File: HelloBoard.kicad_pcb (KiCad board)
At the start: 2 copper layers, 106.3 x 77 mm, 52 parts, among them J1 USB_B_Micro, J2 Conn_01x04_Pin, J3 Conn_01x04_Pin, J4 Conn_02x08_Top_Bottom, J5 Conn_01x02, SW1 SW_Push, SW2 SW_Push, U1 STM32F103C8T6, U2 AMS1117-3.3, U3 TMP235A2DCKR, U4 ADXL343, Y1 16MHz

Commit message: about to run DRC
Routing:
- net /PC_14: track 6.47 -> 71.3 mm, vias 0 -> 10
- net /PC_15: track 6.70 -> 66.6 mm, vias 0 -> 12
- net /PA_9: track 0.00 -> 53.5 mm, vias 0 -> 7
- net /PB_5: track 0.00 -> 50.4 mm, vias 0 -> 4
- net /PA_10: track 0.00 -> 47.8 mm, vias 0 -> 6
- net /PB_4: track 0.00 -> 45.1 mm, vias 0 -> 4
- net /PB_3: track 0.00 -> 40.2 mm, vias 0 -> 6
- net +3.3V: track 266.7 -> 270.2 mm

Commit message: the router ?
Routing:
- net unconnected-(J1-Shield-Pad6)_2: track 0.00 -> 18.0 mm, vias 0 -> 3
- net /PA_10: track 47.8 -> 49.3 mm
- net /PA_9: track 53.5 -> 55.0 mm, vias 7 -> 6
- net /7SEG_A: vias 3 -> 2

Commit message: minor silkscreen edits
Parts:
- renumbered SW1 to NRST
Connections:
- net Net-(J5-Pin_1) renamed /ADXL_INT1
- net Net-(J5-Pin_2) renamed /ADXL_INT2
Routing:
- net unconnected-(J1-Shield-Pad6)_2: track 18.0 -> 0.16 mm, vias 3 -> 0
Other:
- board text added: "16x2 LCD"
- board text added: "3.3V"
- board text added: "5V"
- board text added: "7 SEGMENT DISPLAY"
- board text added: "ADXL343"
- board text added: "GND"
- board text added: "INT1"
- board text added: "INT2"
- board text added: "LCD CONTRAST"
- board text added: "PA10"
- board text added: "PA11"
- board text added: "PA12"
- board text added: "PA7"
- board text added: "PA8"
- board text added: "PA9"
- board text added: "PB1"
- board text added: "PB2"
- board text added: "PB3"
- board text added: "PB4"
- board text added: "PB5"
- board text added: "PC14"
- board text added: "PC15"
- board text added: "SCL"
- board text added: "SDA"
- board text added: "SWCLK"
- board text added: "SWDIO"
- board text added: "TMP235"
- board text added: "USER BUTTON"

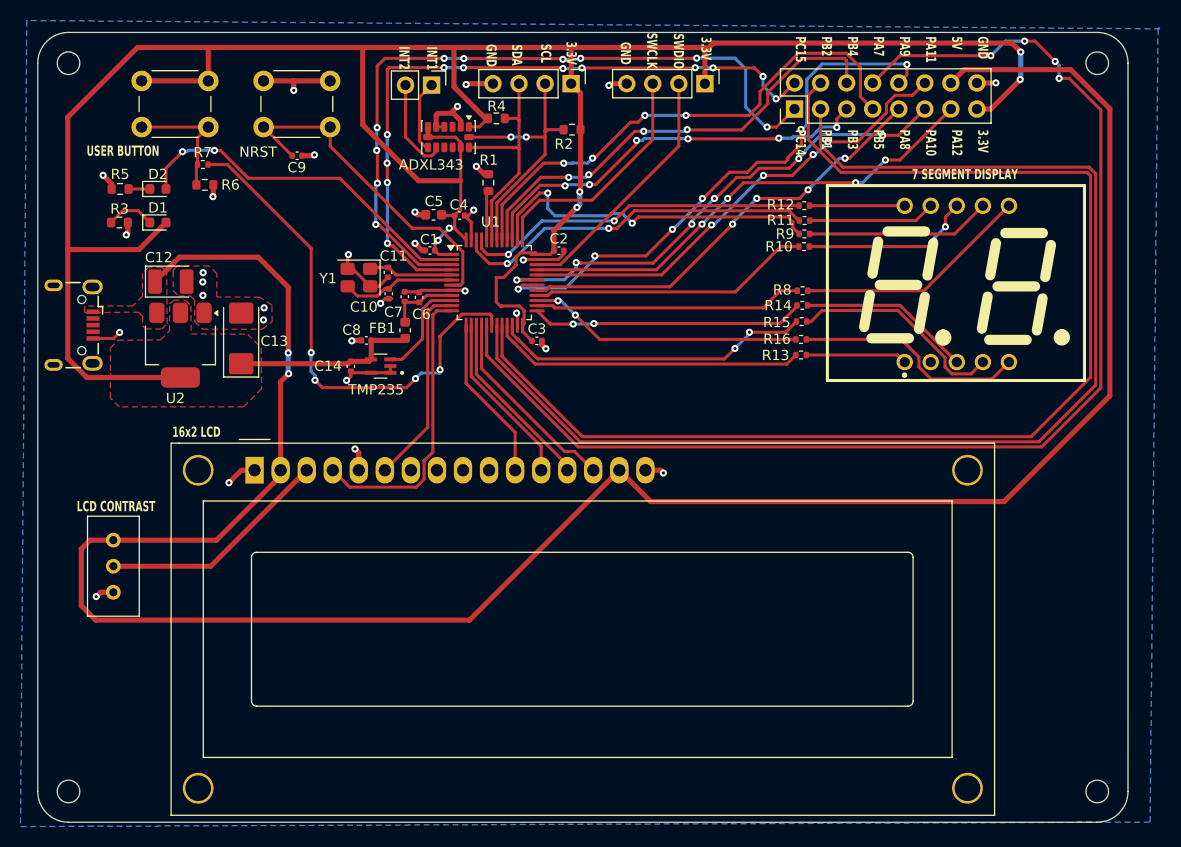
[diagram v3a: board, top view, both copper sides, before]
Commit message: minor via edits
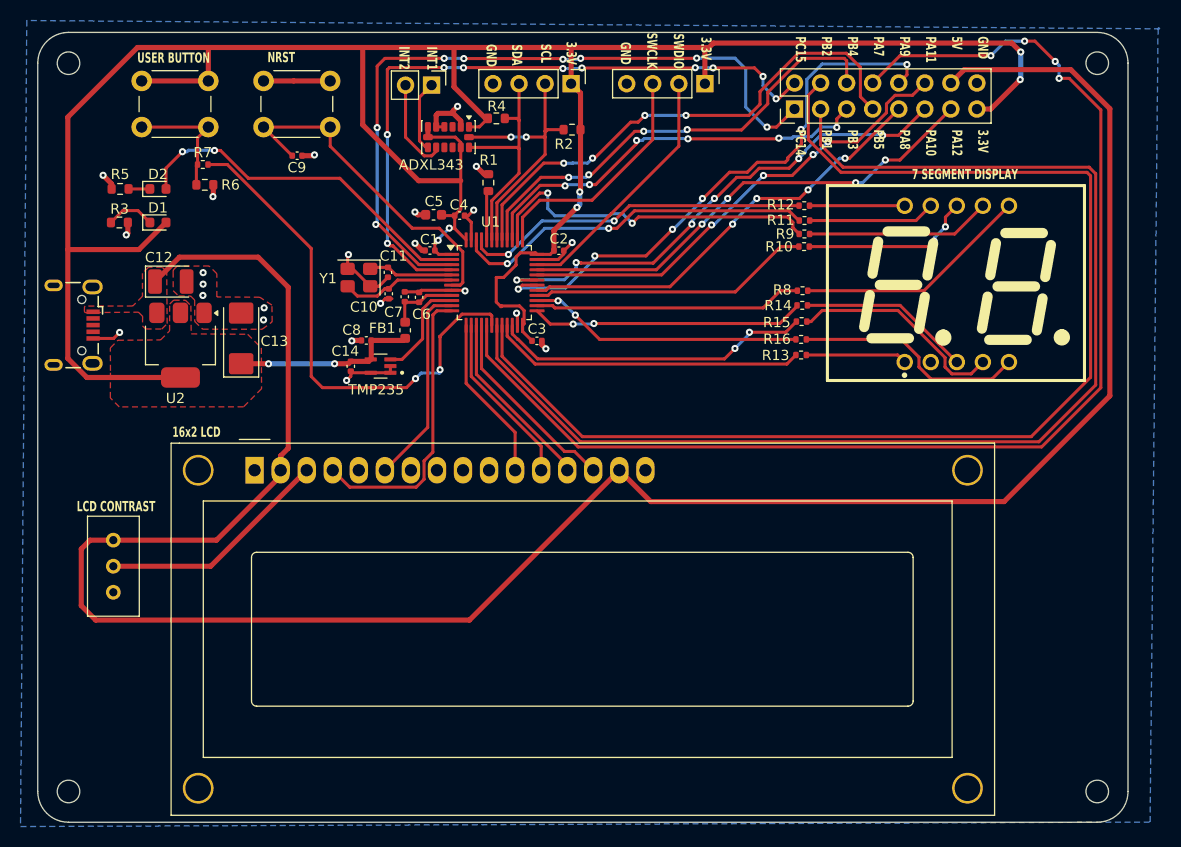
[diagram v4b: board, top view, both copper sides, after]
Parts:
- renumbered NRST to SW1
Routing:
- net GND: track 71.7 -> 55.3 mm, vias 31 -> 23
- net VBUS: vias 2 -> 0
- net /PC_15: vias 12 -> 10
- net +3.3V: vias 6 -> 8
- net /USER_BUTTON: vias 4 -> 2
- net /PC_14: vias 10 -> 8
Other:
- board text added: "NRST"

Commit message: stuck with the ams1117-3.3
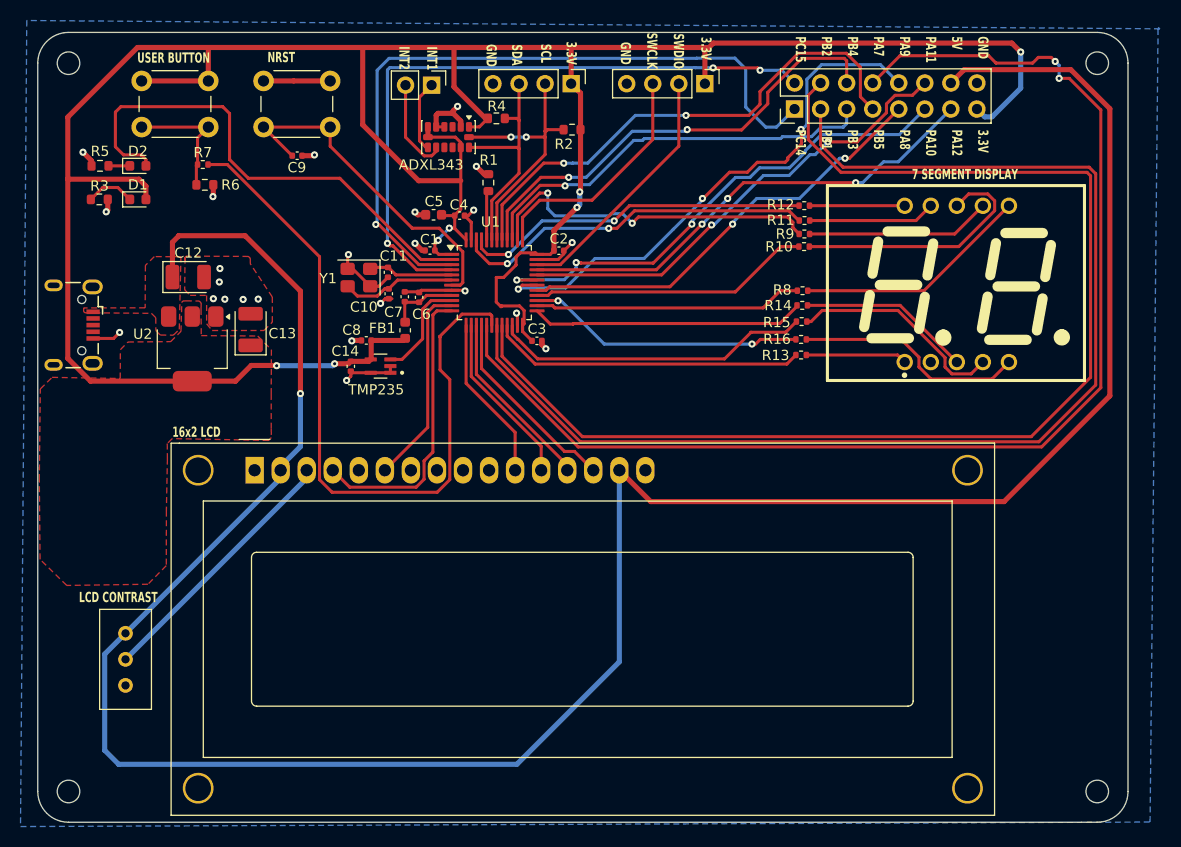
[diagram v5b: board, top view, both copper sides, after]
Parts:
- C13: footprint Capacitor_Tantalum_SMD:CP_EIA-6032-15_Kemet-U -> Capacitor_Tantalum_SMD:CP_EIA-3528-21_Kemet-B
- moved RV1 9.16 mm to (124.1, 96.6)
- moved D1 2.98 mm to (125.3, 54.3)
- moved D2 2.98 mm to (125.3, 51.0)
- moved R5 2.98 mm to (121.7, 51.0)
- moved R3 2.98 mm to (121.6, 54.3)
- moved C12 1.76 mm to (130.3, 61.8)
- moved C13 1.26 mm to (136.3, 67.0)
- moved U2 1.21 mm to (130.7, 68.8)
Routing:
- net VBUS: track 219.9 -> 243.6 mm, vias 0 -> 1
- net /USER_BUTTON: track 50.1 -> 71.4 mm, vias 2 -> 0
- net /USER_LED: track 35.0 -> 49.3 mm, vias 2 -> 0
- net /D1_CA: track 16.8 -> 24.9 mm, vias 2 -> 0
- net +3.3V: track 270.2 -> 276.6 mm, vias 8 -> 7
- net /LCD_VO: track 22.7 -> 26.5 mm
- net /PA_9: track 55.0 -> 52.6 mm, vias 6 -> 3
- net /PC_15: track 66.6 -> 64.6 mm, vias 10 -> 3
- net /PA_7: track 123.4 -> 122.7 mm, vias 4 -> 2
- net /PC_14: track 71.3 -> 71.0 mm, vias 8 -> 1
- net /PB_3: track 40.2 -> 40.3 mm, vias 6 -> 1
- net /7SEG_D: track 31.2 -> 31.1 mm, vias 2 -> 0
- net /PA_10: vias 6 -> 3
- net /PB_4: track 45.1 -> 45.0 mm, vias 4 -> 2
- net /PB_5: vias 4 -> 2
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
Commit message: .
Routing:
- net GND: track 55.3 -> 56.0 mm
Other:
- board text added: "16 MHz Crystal"
- board text added: "ADXL Interrupts"
- board text added: "AMS1117"
- board text added: "GPIO Header"
- board text added: "I2C Header"
- board text added: "STM32F103C8T6"
- board text added: "SWD Header"
- board text added: "USB B Micro"
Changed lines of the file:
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@@
 		(tags "capacitor")
 		(property "Reference" "C11"
-			(at -1.6 -0.54 180)
+			(at -0.34 -1.84 180)
 			(layer "F.SilkS")
 			(effects
@@
 		(tags "resistor")
 		(property "Reference" "R4"
-			(at 0.03 -1.19 0)
+			(at -0.1 1.26 0)
 			(layer "F.SilkS")
 			(effects
@@
 			(at -0.3725 -5.92 0)
 			(layer "F.SilkS")
+			(hide yes)
 			(effects
 				(font
@@
 		)
 	)
+	(gr_text "ADXL Interrupts"
+		(at 148.38 46.15 0)
+		(layer "F.SilkS")
+		(effects
+			(font
+				(size 1 0.65)
+				(thickness 0.15)
+				(bold yes)
+			)
+			(justify left bottom)
+		)
+	)
+	(gr_text "I2C Header"
+		(at 163.27 45.94 0)
+		(layer "F.SilkS")
+		(effects
+			(font
+				(size 1 0.65)
+				(thickness 0.15)
+				(bold yes)
+			)
+			(justify left bottom)
+		)
+	)
+	(gr_text "SWD Header"
+		(at 176.7 45.94 0)
+		(layer "F.SilkS")
+		(effects
+			(font
+				(size 1 0.65)
+				(thickness 0.15)
+				(bold yes)
+			)
+			(justify left bottom)
+		)
+	)
 	(gr_text "7 SEGMENT DISPLAY"
 		(at 200.81 52.41 0)
@@
 		)
 	)
+	(gr_text "GPIO Header"
+		(at 209.32 44.44 0)
+		(layer "F.SilkS")
+		(effects
+			(font
+				(size 1 0.65)
+				(thickness 0.15)
+				(bold yes)
+			)
+			(justify left bottom)
+		)
+	)
 	(gr_text "INT2"
 		(at 150.72 39.34 270)
@@
 		)
 	)
+	(gr_text "USB B Micro"
+		(at 120.5 60.66 0)
+		(layer "F.SilkS")
+		(effects
+			(font
+				(size 1 1)
+				(thickness 0.15)
+			)
+		)
+	)
+	(gr_text "AMS1117"
+		(at 130.83 74.31 0)
+		(layer "F.SilkS")
+		(effects
+			(font
+				(size 1 1)
+				(thickness 0.15)
+			)
+		)
+	)
+	(gr_text "16 MHz Crystal"
+		(at 145.93 59.42 0)
+		(layer "F.SilkS")
+		(effects
+			(font
+				(size 1 1)
+				(thickness 0.15)
+			)
+		)
+	)
 	(gr_text "TMP235"
 		(at 148.58 72.82 0)
@@
 		)
 	)
+	(gr_text "STM32F103C8T6"
+		(at 159.95 69.18 0)
+		(layer "F.SilkS")
+		(effects
+			(font
+				(size 1 1)
+				(thickness 0.15)
+			)
+		)
+	)
 	(segment
 		(start 157.19 63.13)
@@
 	)
 	(segment
+		(start 145.8 61.04)
+		(end 144.27 61.04)
+		(width 0.3)
+		(layer "F.Cu")
+		(net 1)
+	)
+	(segment
 		(start 157.8525 58.2175)
 		(end 157.8525 56.5025)
@@
 	)
 	(segment
-		(start 145.8 61.04)
-		(end 145.8 59.73)
-		(width 0.3)
-		(layer "F.Cu")
-		(net 1)
-	)
-	(segment
 		(start 166.875 59.579999)
 		(end 166.875 59.27)
@@
 	)
 	(segment
-		(start 164.735 68.435)
-		(end 165.13 68.83)
-		(width 0.5)
-		(layer "F.Cu")
-		(net 1)
-	)
-	(segment
 		(start 162.3525 66.5425)
 		(end 162.3525 65.439914)
@@
 	)
 	(segment
+		(start 164.735 68.06)
+		(end 165.93 68.06)
+		(width 0.5)
+		(layer "F.Cu")
+		(net 1)
+	)
+	(segment
 		(start 156.09 45.88)
 		(end 156.09 45.63)
@@
 	)
 	(segment
+		(start 165.93 68.06)
+		(end 166.03 67.96)
+		(width 0.5)
+		(layer "F.Cu")
+		(net 1)
+	)
+	(segment
 		(start 149.81 63.95)
 		(end 149.47 63.95)
@@
 	)
 	(segment
+		(start 144.27 61.04)
+		(end 144.09 60.86)
+		(width 0.3)
+		(layer "F.Cu")
+		(net 1)
+	)
+	(segment
 		(start 149.97 70.52)
 		(end 149.97 71.17)
@@
 	)
 	(segment
-		(start 145.8 59.73)
-		(end 145.88 59.65)
-		(width 0.3)
-		(layer "F.Cu")
-		(net 1)
-	)
-	(segment
 		(start 157.55 55.85)
 		(end 158.09 55.31)
@@
 	)
 	(segment
-		(start 164.735 68.06)
-		(end 164.735 68.435)
-		(width 0.5)
-		(layer "F.Cu")
-		(net 1)
-	)
-	(segment
 		(start 122.4175 54.27)
 		(end 122.4175 55.325)
@@
 	)
 	(via
-		(at 145.88 59.65)
-		(size 0.7)
-		(drill 0.3)
-		(layers "F.Cu" "B.Cu")
-		(net 1)
-	)
-	(via
 		(at 152.36 55.5)
 		(size 0.7)
@@
 	)
 	(via
+		(at 144.09 60.86)
+		(size 0.7)
+		(drill 0.3)
+		(layers "F.Cu" "B.Cu")
+		(net 1)
+	)
+	(via
 		(at 152.37 58.55)
 		(size 0.7)
@@
 	)
 	(via
-		(at 120 49.67)
+		(at 166.03 67.96)
 		(size 0.7)
 		(drill 0.3)
@@
 	)
 	(via
-		(at 123.57 67.24)
+		(at 120 49.67)
 		(size 0.7)
 		(drill 0.3)
@@
 	)
 	(via
-		(at 165.13 68.83)
+		(at 123.57 67.24)
 		(size 0.7)
 		(drill 0.3)
@@
 	)
 	(segment
-		(start 184.922894 46.08)
-		(end 186.001447 45.001447)
+		(start 195.79 44.26)
+		(end 196.99 45.46)
 		(width 0.3)
 		(layer "F.Cu")
@@
 	)
 	(segment
-		(start 186.001447 45.001447)
-		(end 186.001447 43.758553)
+		(start 160.8525 54.80007)
+		(end 164.92257 50.73)
 		(width 0.3)
 		(layer "F.Cu")
@@
 	)
 	(segment
-		(start 186.001447 43.758553)
-		(end 189.74 40.02)
+		(start 184.372894 46.63)
+		(end 186.001447 45.001447)
 		(width 0.3)
 		(layer "F.Cu")
@@
 	)
 	(segment
-		(start 160.8525 54.80007)
-		(end 164.92257 50.73)
+		(start 164.92257 50.73)
+		(end 166.86 50.73)
 		(width 0.3)
 		(layer "F.Cu")
@@
 	)
 	(segment
-		(start 164.92257 50.73)
-		(end 166.86 50.73)
+		(start 194.417106 40.02)
+		(end 195.79 41.392894)
 		(width 0.3)
 		(layer "F.Cu")
@@
 	)
 	(segment
-		(start 195.79 44.26)
-		(end 196.99 45.46)
+		(start 166.86 50.73)
+		(end 166.87 50.74)
 		(width 0.3)
 		(layer "F.Cu")
@@
 	)
 	(segment
-		(start 166.86 50.73)
-		(end 166.87 50.74)
+		(start 186.001447 45.001447)
+		(end 186.001447 43.758553)
 		(width 0.3)
 		(layer "F.Cu")
@@
 	)
 	(segment
-		(start 194.417106 40.02)
-		(end 195.79 41.392894)
+		(start 189.74 40.02)
+		(end 194.417106 40.02)
 		(width 0.3)
 		(layer "F.Cu")
@@
 	)
 	(segment
-		(start 178.79 46.08)
-		(end 184.922894 46.08)
+		(start 182.78 46.63)
+		(end 184.372894 46.63)
 		(width 0.3)
 		(layer "F.Cu")
@@
 	)
 	(segment
-		(start 189.74 40.02)
-		(end 194.417106 40.02)
+		(start 160.8525 58.2175)
+		(end 160.8525 54.80007)
 		(width 0.3)
 		(layer "F.Cu")
@@
 	)
 	(segment
-		(start 160.8525 58.2175)
-		(end 160.8525 54.80007)
+		(start 186.001447 43.758553)
+		(end 189.74 40.02)
 		(width 0.3)
 		(layer "F.Cu")
@@
 	)
 	(via
-		(at 178.79 46.08)
+		(at 182.78 46.63)
 		(size 0.7)
 		(drill 0.3)
@@
 	)
 	(segment
-		(start 173.855 46.08)
-		(end 178.79 46.08)
+		(start 173.64 46.63)
+		(end 182.78 46.63)
 		(width 0.3)
 		(layer "B.Cu")
@@
 	)
 	(segment
-		(start 167.755 50.73)
-		(end 169.205 50.73)
+		(start 167.745 50.74)
+		(end 167.755 50.73)
 		(width 0.3)
 		(layer "B.Cu")
@@
 	)
 	(segment
-		(start 166.87 50.74)
-		(end 167.745 50.74)
+		(start 169.54 50.73)
+		(end 173.64 46.63)
 		(width 0.3)
 		(layer "B.Cu")
@@
 	)
 	(segment
-		(start 169.205 50.73)
-		(end 173.855 46.08)
+		(start 167.755 50.73)
+		(end 169.54 50.73)
 		(width 0.3)
 		(layer "B.Cu")
@@
 	)
 	(segment
-		(start 167.745 50.74)
-		(end 167.755 50.73)
+		(start 166.87 50.74)
+		(end 167.745 50.74)
 		(width 0.3)
 		(layer "B.Cu")

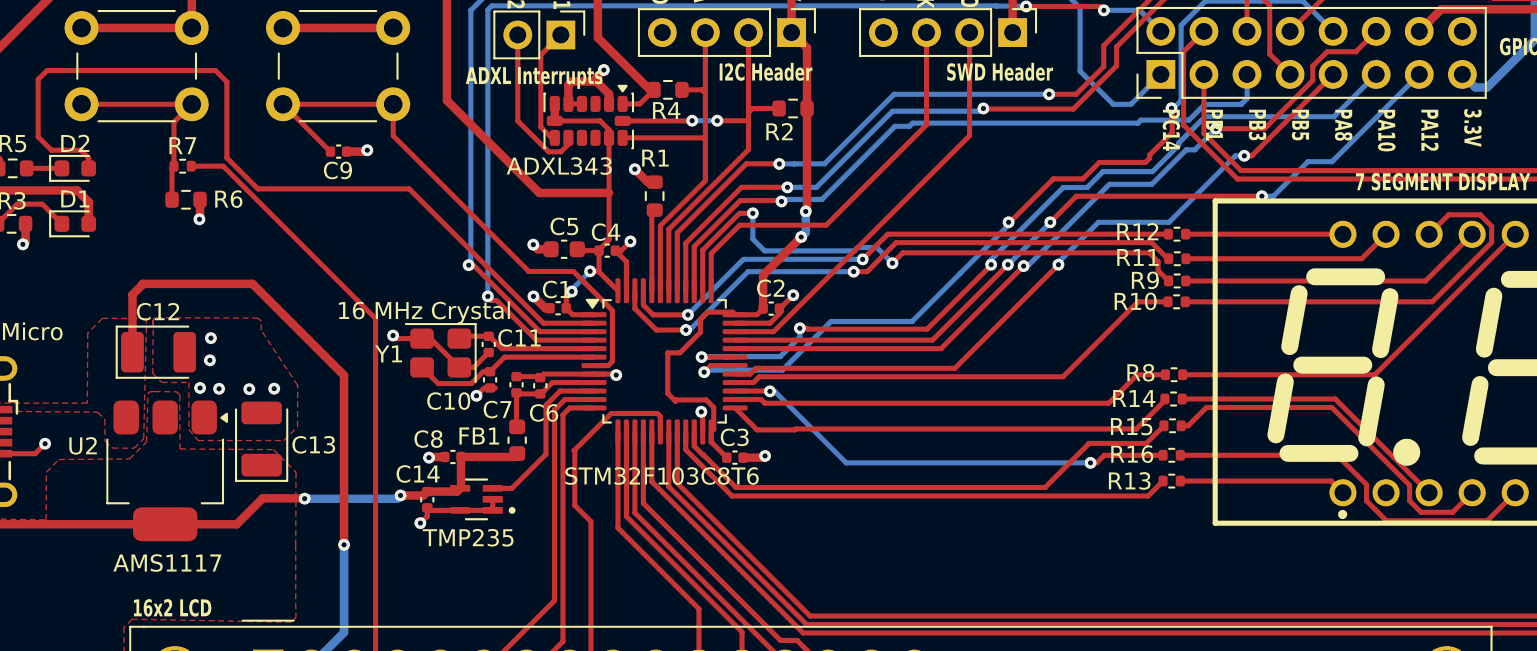
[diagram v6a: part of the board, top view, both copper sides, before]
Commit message: TODO 7segment digit control
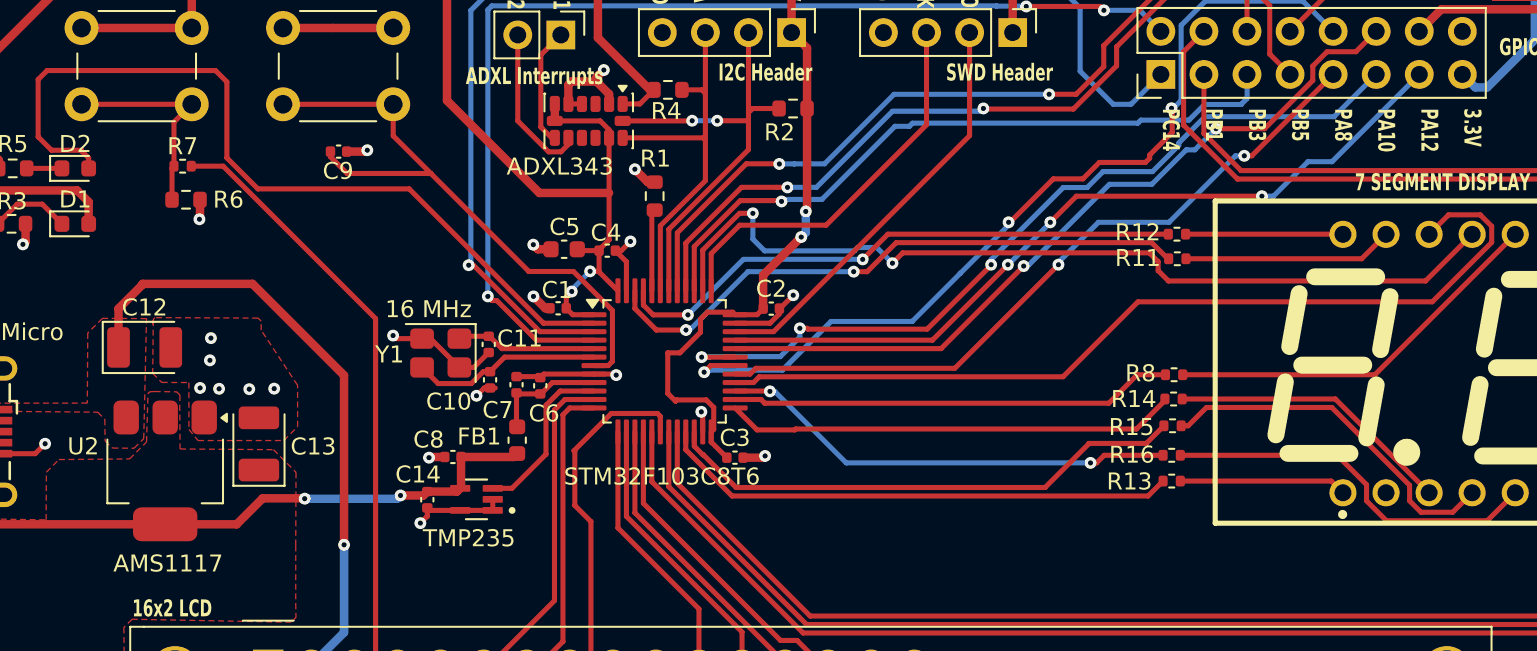
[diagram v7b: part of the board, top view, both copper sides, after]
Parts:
- removed R10, R9: 220, Resistor_SMD:R_0402_1005Metric
- C12: value 10u -> 10uF
- C13: value 22u -> 22uF
- moved C12 0.87 mm to (129.4, 61.6)
- moved C13 0.33 mm to (136.2, 67.2)
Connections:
- LED1 pad 7: /D2_CA -> /7SEG_D2_CA
- LED1 pad 8: /D1_CA -> /7SEG_D1_CA
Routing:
- net /7SEG_D1_CA: track 27.5 -> 53.4 mm
- net /D1_CA: track 24.9 -> 0.00 mm
- net /7SEG_D2_CA: track 34.3 -> 53.3 mm
- net /D2_CA: track 18.0 -> 0.00 mm
- net /NRST: track 33.7 -> 36.4 mm
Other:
- board text added: "16 MHz"
- board text removed: "16 MHz Crystal"

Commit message: board finished (for now)
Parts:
- added Q1: AO3401A, Package_TO_SOT_SMD:SOT-23, F.Cu at (190.0, 59.8)
- added Q2: AO3401A, Package_TO_SOT_SMD:SOT-23, F.Cu at (190.0, 64.3)
- added R10: 1K, Resistor_SMD:R_0603_1608Metric, F.Cu at (183.9, 64.4)
- added R17: 10k, Resistor_SMD:R_0603_1608Metric, F.Cu at (186.6, 59.9)
- added R18: 10k, Resistor_SMD:R_0603_1608Metric, F.Cu at (186.6, 64.3)
- added R9: 1K, Resistor_SMD:R_0603_1608Metric, F.Cu at (183.9, 60.1)
- R3, R5: value 1K5 -> 1K
- moved R13 5.80 mm to (190.3, 75.2)
- moved R14 5.80 mm to (190.4, 70.4)
- moved R16 5.80 mm to (190.3, 73.7)
- moved R15 5.80 mm to (190.3, 72.0)
- moved R8 5.80 mm to (190.4, 69.0)
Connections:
- U1 pad 28: /7SEG_D1_CA -> /D1_CA
- U1 pad 38: /7SEG_D2_CA -> /D2_CA
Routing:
- net +3.3V: track 276.6 -> 336.4 mm, vias 7 -> 9
- net /7SEG_D1_CA: track 53.4 -> 16.3 mm
- net /7SEG_D2_CA: track 53.3 -> 20.7 mm, vias 2 -> 0
- net /D2_CA: track 0.00 -> 31.3 mm, vias 0 -> 2
- net /D1_CA: track 0.00 -> 20.8 mm
- net /Gate_Q1: track 0.00 -> 5.31 mm
- net /Gate_Q2: track 0.00 -> 5.24 mm
- net /7SEG_G: track 27.2 -> 29.5 mm
- net /G: track 22.6 -> 24.9 mm
- net /F: track 23.0 -> 25.2 mm
- net /7SEG_C: track 30.7 -> 32.6 mm
- net /C: track 9.88 -> 11.4 mm
- net /7SEG_F: track 26.2 -> 27.4 mm
- net /7SEG_E: track 26.7 -> 27.8 mm
- net /PA_9: track 52.6 -> 52.5 mm, vias 3 -> 5
